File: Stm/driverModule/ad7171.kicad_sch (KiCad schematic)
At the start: 8 parts, among them J6 Conn_01x04, U4 AD7171, U5 AD7171, U6 AD8629ARZ-REEL

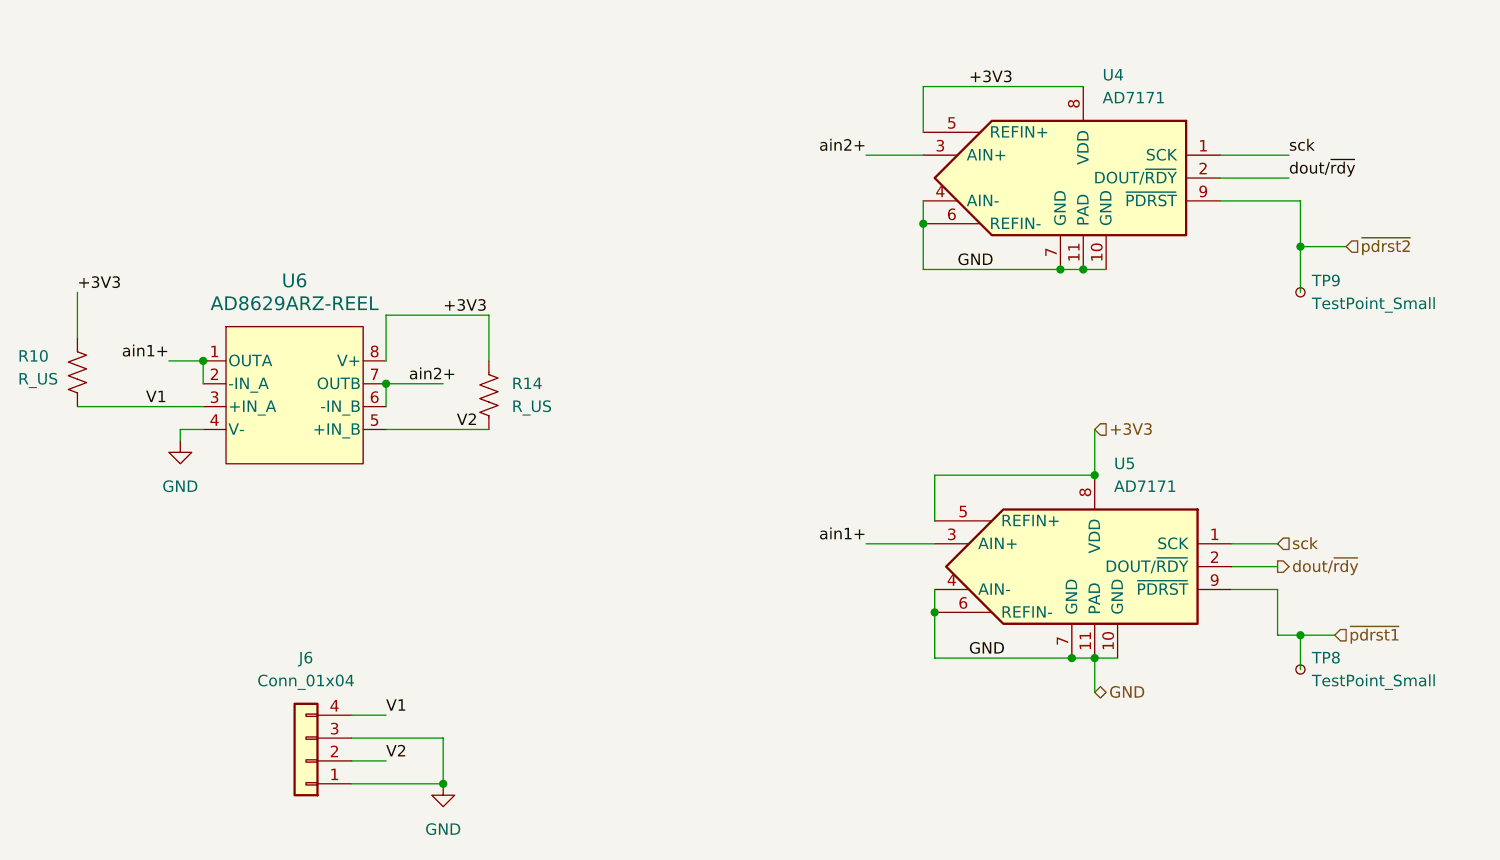
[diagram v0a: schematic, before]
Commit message: Capacitors
Added some filter capacitors
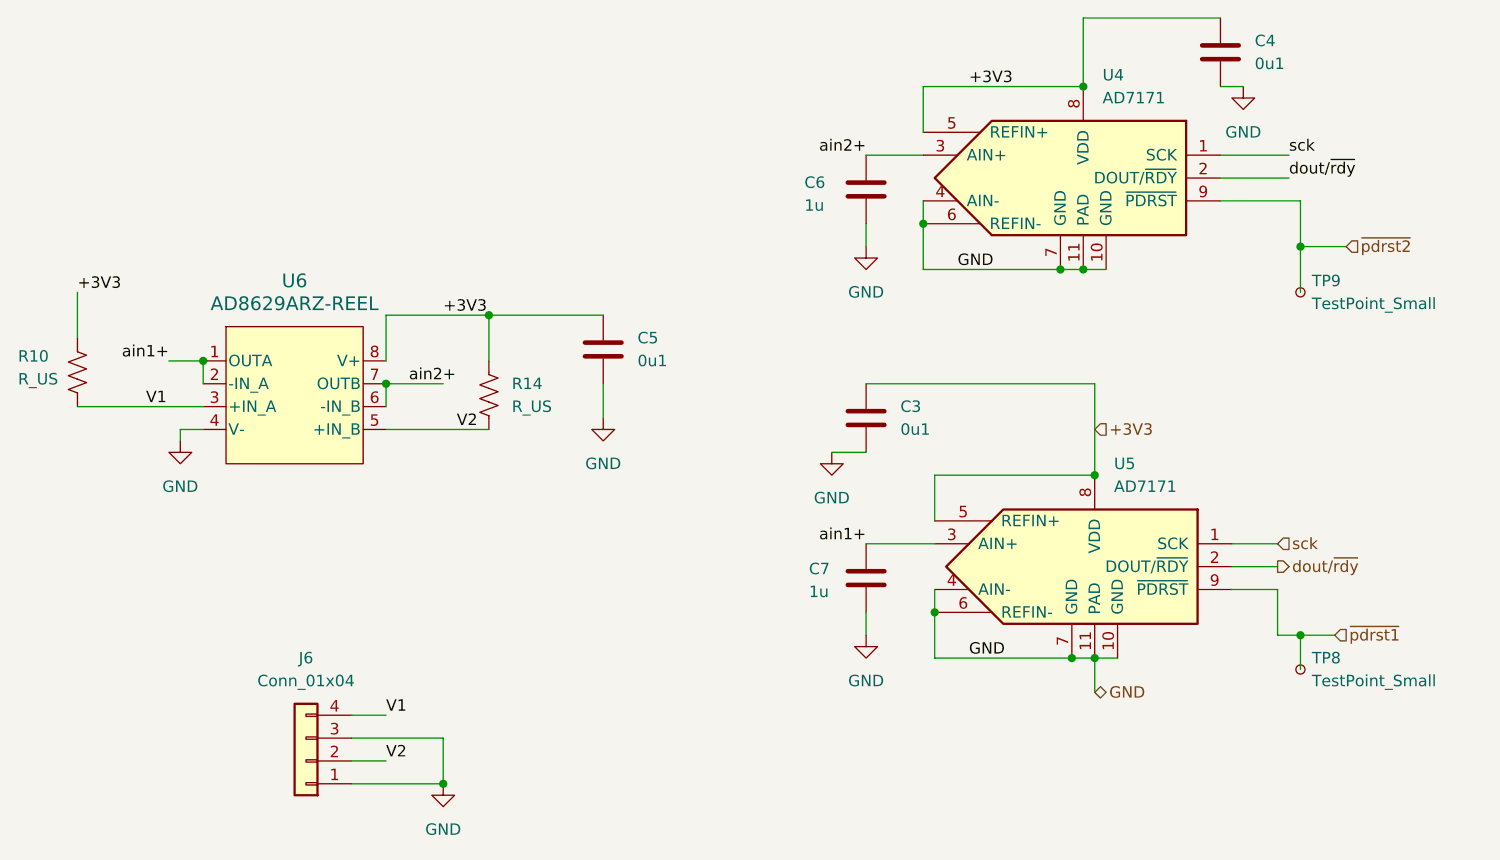
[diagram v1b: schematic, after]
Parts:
- added C3, C4, C5: 0u1, Capacitor_SMD:C_0402_1005Metric_Pad0.74x0.62mm_HandSolder, symbol Device:C
- added C6, C7: 1u, Capacitor_SMD:C_0402_1005Metric_Pad0.74x0.62mm_HandSolder, symbol Device:C
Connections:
- net +3V3: now also C3.1, C4.1, C5.1
- net GND: now also C3.2, C4.2, C5.2, C6.2, C7.2
- net ain1+: now also C7.1
- net ain2+: now also C6.1
